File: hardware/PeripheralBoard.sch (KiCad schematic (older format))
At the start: 23 parts, among them J1 PARAM1_CV, J2 PARAM2_CV, J3 CLK/TRG, J4 DITTO, J5 OUT1, J6 OUT2, J7 B1_HDR_LEFT, J8 B1_HDR_RIGHT

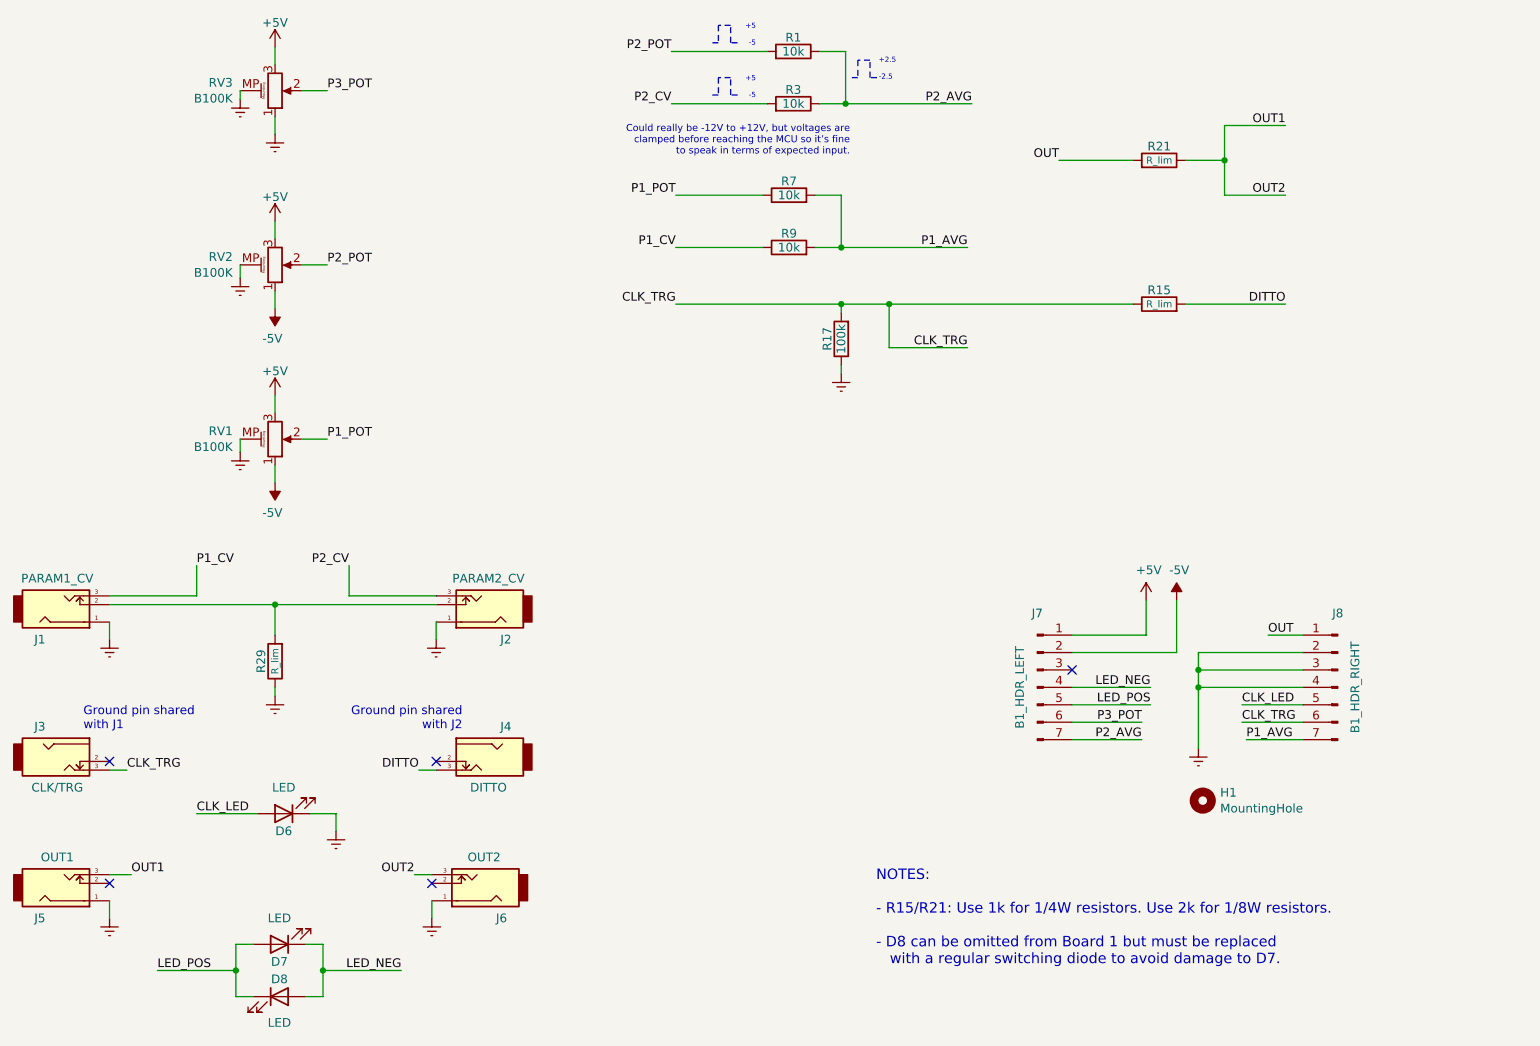
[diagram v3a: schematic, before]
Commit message: [JNTUB-HW] PCB now preparable for SMT assembly!
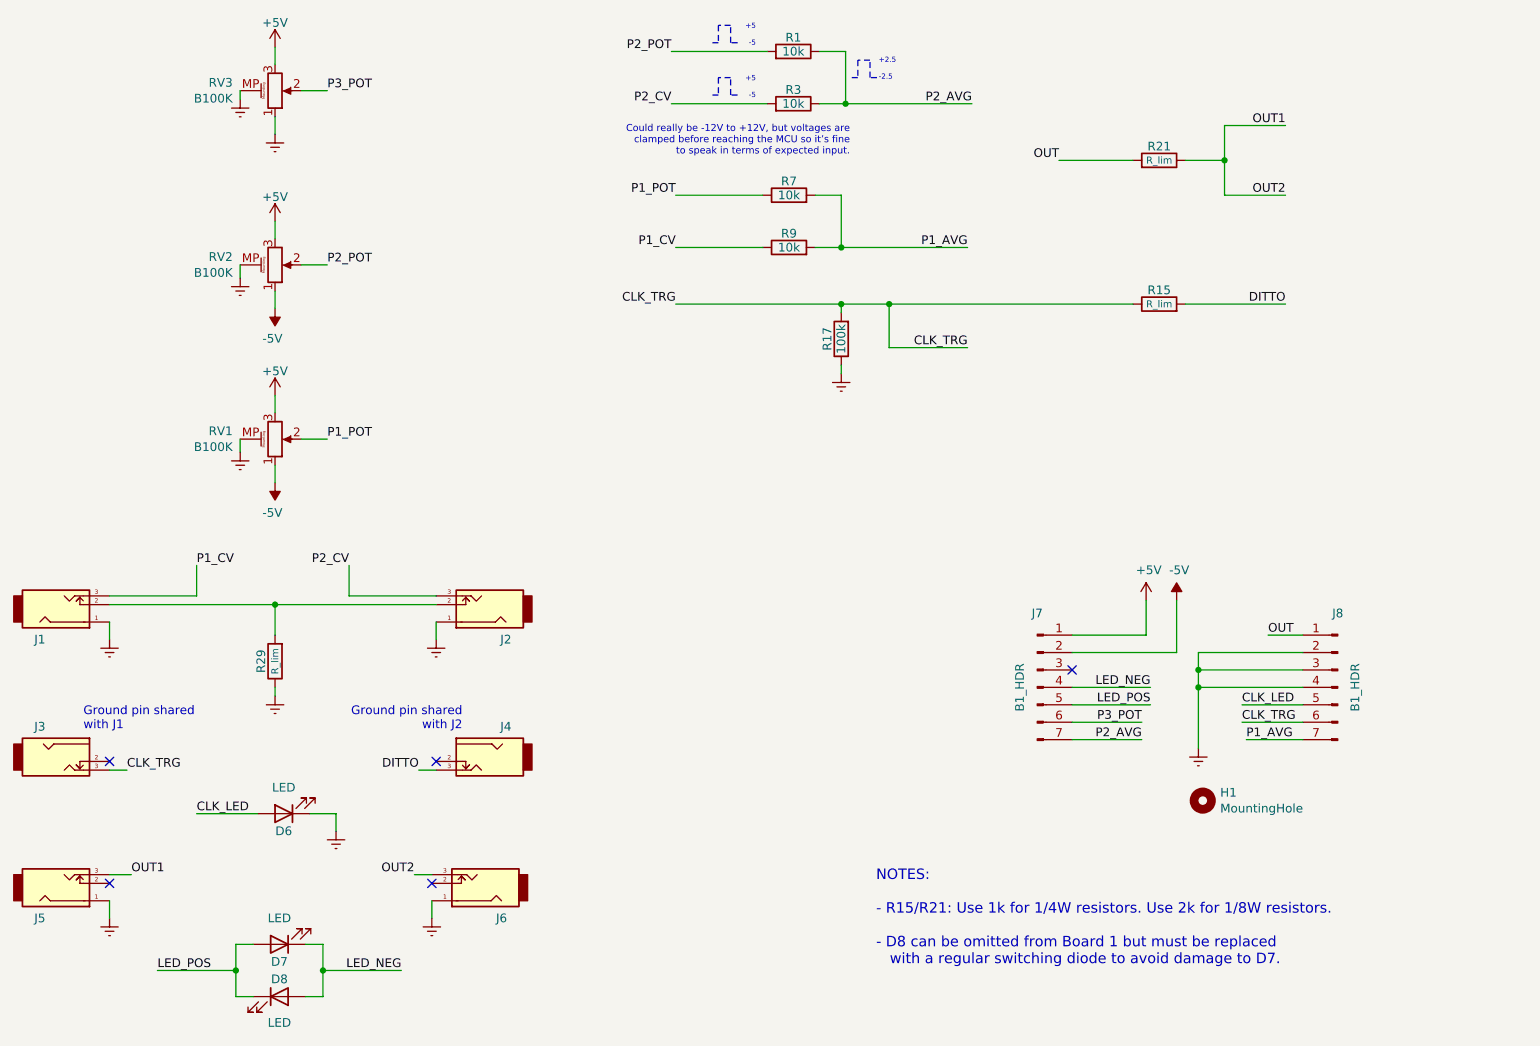
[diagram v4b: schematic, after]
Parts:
- D6, D7, D8: Config (none) -> -smtmfg; Type (none) -> 3mm LED
- H1: Config (none) -> do not fit; Exclude (none) -> Yes
- J1: value PARAM1_CV -> 3.5mm Mono Jack; Config (none) -> -smtmfg; Type (none) -> Thonkiconn Jack
- J2: value PARAM2_CV -> 3.5mm Mono Jack; Config (none) -> -smtmfg; Type (none) -> Thonkiconn Jack
- J3: value CLK/TRG -> 3.5mm Mono Jack; Config (none) -> -smtmfg; Type (none) -> Thonkiconn Jack
- J4: value DITTO -> 3.5mm Mono Jack; Config (none) -> -smtmfg; Type (none) -> Thonkiconn Jack
- J5: value OUT1 -> 3.5mm Mono Jack; Config (none) -> -smtmfg; Type (none) -> Thonkiconn Jack
- J6: value OUT2 -> 3.5mm Mono Jack; Config (none) -> -smtmfg; Type (none) -> Thonkiconn Jack
- J7: value B1_HDR_LEFT -> B1_HDR; Config (none) -> -smtmfg; Type (none) -> 1x7 Male Pin Header
- J8: value B1_HDR_RIGHT -> B1_HDR; Config (none) -> -smtmfg; Type (none) -> 1x7 Male Pin Header
- R1, R3, R7, R9: LCSC (none) -> C17414; SMT Place (none) -> Yes; SMT package (none) -> R_0805; Tolerance (none) -> 1%; Type (none) -> 1% Metal Film Resistor
- R15, R21, R29: LCSC (none) -> C4410; Note (none) -> Use 1k 1/4W or 2k 1/8W; Power Rating (none) -> 1/4W; SMT Note (none) -> 1206 1/4W; SMT Place (none) -> Yes; SMT package (none) -> R_0805 or R_1206; Type (none) -> 5% Resistor
- R17: LCSC (none) -> C17407; SMT Place (none) -> Yes; SMT package (none) -> R_0805; Type (none) -> 5% Carbon Film Resistor
- RV1, RV2, RV3: Config (none) -> -smtmfg; Type (none) -> Alpha 9mm Vertical Potentiometer
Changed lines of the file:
@@
 F 2 "SDIY:Potentiometer_Alpha_9mm_WithGround" H 3250 1450 50  0001 C CNN
 F 3 "" H 3250 1450 50  0001 C CNN
+F 4 "" H 3250 1450 50  0001 C CNN "Part"
+F 5 "-smtmfg" H 3250 1450 50  0001 C CNN "Config"
+F 6 "Alpha 9mm Vertical Potentiometer" H 3250 1450 50  0001 C CNN "Type"
 	1    3250 1450
 	1    0    0    1
@@
 F 2 "SDIY:Potentiometer_Alpha_9mm_WithGround" H 3250 2450 50  0001 C CNN
 F 3 "" H 3250 2450 50  0001 C CNN
+F 4 "" H 3250 2450 50  0001 C CNN "Part"
+F 5 "-smtmfg" H 3250 2450 50  0001 C CNN "Config"
+F 6 "Alpha 9mm Vertical Potentiometer" H 3250 2450 50  0001 C CNN "Type"
 	1    3250 2450
 	1    0    0    1
@@
 P 1850 4400
 F 0 "J1" H 1900 4200 50  0000 C CNN
-F 1 "PARAM1_CV" H 2000 4550 50  0000 C CNN
+F 1 "3.5mm Mono Jack" H 2000 4550 50  0001 C CNN
 F 2 "SDIY:PJ301M-12_Thonkiconn" H 1850 4400 50  0001 C CNN
 F 3 "" H 1850 4400 50  0001 C CNN
+F 4 "" H 1850 4400 50  0001 C CNN "Part"
+F 5 "-smtmfg" H 1850 4400 50  0001 C CNN "Config"
+F 6 "Thonkiconn Jack" H 1850 4400 50  0001 C CNN "Type"
 	1    1850 4400
 	1    0    0    -1
@@
 F 2 "SDIY:Potentiometer_Alpha_9mm_WithGround" H 3250 3450 50  0001 C CNN
 F 3 "" H 3250 3450 50  0001 C CNN
+F 4 "" H 3250 3450 50  0001 C CNN "Part"
+F 5 "-smtmfg" H 3250 3450 50  0001 C CNN "Config"
+F 6 "Alpha 9mm Vertical Potentiometer" H 3250 3450 50  0001 C CNN "Type"
 	1    3250 3450
 	1    0    0    1
@@
 P 4625 4400
 F 0 "J2" H 4675 4200 50  0000 C CNN
-F 1 "PARAM2_CV" H 4775 4550 50  0000 C CNN
+F 1 "3.5mm Mono Jack" H 4775 4550 50  0001 C CNN
 F 2 "SDIY:PJ301M-12_Thonkiconn" H 4625 4400 50  0001 C CNN
 F 3 "" H 4625 4400 50  0001 C CNN
+F 4 "" H 4625 4400 50  0001 C CNN "Part"
+F 5 "-smtmfg" H 4625 4400 50  0001 C CNN "Config"
+F 6 "Thonkiconn Jack" H 4625 4400 50  0001 C CNN "Type"
 	1    4625 4400
 	-1   0    0    -1
@@
 P 4625 5300
 F 0 "J4" H 4675 5100 50  0000 C CNN
-F 1 "DITTO" H 4775 5450 50  0000 C CNN
+F 1 "3.5mm Mono Jack" H 4775 5450 50  0001 C CNN
 F 2 "SDIY:PJ301M-12_Thonkiconn_NoGround" H 4625 5300 50  0001 C CNN
 F 3 "" H 4625 5300 50  0001 C CNN
+F 4 "" H 4625 5300 50  0001 C CNN "Part"
+F 5 "-smtmfg" H 4625 5300 50  0001 C CNN "Config"
+F 6 "Thonkiconn Jack" H 4625 5300 50  0001 C CNN "Type"
 	1    4625 5300
 	-1   0    0    1
@@
 P 1850 6000
 F 0 "J5" H 1900 5800 50  0000 C CNN
-F 1 "OUT1" H 2000 6150 50  0000 C CNN
+F 1 "3.5mm Mono Jack" H 2000 6150 50  0001 C CNN
 F 2 "SDIY:PJ301M-12_Thonkiconn" H 1850 6000 50  0001 C CNN
 F 3 "" H 1850 6000 50  0001 C CNN
+F 4 "" H 1850 6000 50  0001 C CNN "Part"
+F 5 "-smtmfg" H 1850 6000 50  0001 C CNN "Config"
+F 6 "Thonkiconn Jack" H 1850 6000 50  0001 C CNN "Type"
 	1    1850 6000
 	1    0    0    -1
@@
 P 4600 6000
 F 0 "J6" H 4650 5800 50  0000 C CNN
-F 1 "OUT2" H 4750 6150 50  0000 C CNN
+F 1 "3.5mm Mono Jack" H 4750 6150 50  0001 C CNN
 F 2 "SDIY:PJ301M-12_Thonkiconn" H 4600 6000 50  0001 C CNN
 F 3 "" H 4600 6000 50  0001 C CNN
+F 4 "" H 4600 6000 50  0001 C CNN "Part"
+F 5 "-smtmfg" H 4600 6000 50  0001 C CNN "Config"
+F 6 "Thonkiconn Jack" H 4600 6000 50  0001 C CNN "Type"
 	1    4600 6000
 	-1   0    0    -1
@@
 F 2 "LEDs:LED_D3.0mm" H 3275 6350 50  0001 C CNN
 F 3 "" H 3275 6350 50  0001 C CNN
+F 4 "" H 3275 6350 50  0001 C CNN "Part"
+F 5 "-smtmfg" H 3275 6350 50  0001 C CNN "Config"
+F 6 "3mm LED" H 3275 6350 50  0001 C CNN "Type"
 	1    3275 6350
 	-1   0    0    1
@@
 F 2 "LEDs:LED_D3.0mm" H 3275 6650 50  0001 C CNN
 F 3 "" H 3275 6650 50  0001 C CNN
+F 4 "" H 3275 6650 50  0001 C CNN "Part"
+F 5 "-smtmfg" H 3275 6650 50  0001 C CNN "Config"
+F 6 "3mm LED" H 3275 6650 50  0001 C CNN "Type"
 	1    3275 6650
 	1    0    0    -1
@@
 F 2 "LEDs:LED_D3.0mm" H 3300 5600 50  0001 C CNN
 F 3 "" H 3300 5600 50  0001 C CNN
+F 4 "" H 3300 5600 50  0001 C CNN "Part"
+F 5 "-smtmfg" H 3300 5600 50  0001 C CNN "Config"
+F 6 "3mm LED" H 3300 5600 50  0001 C CNN "Type"
 	1    3300 5600
 	-1   0    0    1
@@
 AR Path="/5FE9B0F3/61DF2F72" Ref="J7"  Part="1"
 F 0 "J7" H 7625 5300 50  0000 C CNN
-F 1 "B1_HDR_LEFT" V 7525 4875 50  0000 C CNN
+F 1 "B1_HDR" V 7525 4875 50  0000 C CNN
 F 2 "Pin_Headers:Pin_Header_Straight_1x07_Pitch2.54mm" H 7625 4875 50  0001 C CNN
 F 3 "" H 7625 4875 50  0001 C CNN
+F 4 "" H 7625 4875 50  0001 C CNN "Part"
+F 5 "-smtmfg" H 7625 4875 50  0001 C CNN "Config"
+F 6 "1x7 Male Pin Header" H 7625 4875 50  0001 C CNN "Type"
 	1    7625 4875
 	1    0    0    -1
@@
 AR Path="/5FE9B0F3/61DF2F7C" Ref="J8"  Part="1"
 F 0 "J8" H 9350 5300 50  0000 C CNN
-F 1 "B1_HDR_RIGHT" V 9250 4875 50  0000 C CNN
+F 1 "B1_HDR" V 9250 4875 50  0000 C CNN
 F 2 "Pin_Headers:Pin_Header_Straight_1x07_Pitch2.54mm" H 9350 4875 50  0001 C CNN
 F 3 "" H 9350 4875 50  0001 C CNN
+F 4 "" H 9350 4875 50  0001 C CNN "Part"
+F 5 "-smtmfg" H 9350 4875 50  0001 C CNN "Config"
+F 6 "1x7 Male Pin Header" H 9350 4875 50  0001 C CNN "Type"
 	1    9350 4875
 	-1   0    0    -1
@@
 F 2 "Mounting_Holes:MountingHole_3.2mm_M3" H 8575 5525 50  0001 C CNN
 F 3 "~" H 8575 5525 50  0001 C CNN
+F 4 "Yes" H 8575 5525 50  0001 C CNN "Exclude"
+F 5 "do not fit" H 8575 5525 50  0001 C CNN "Config"
 	1    8575 5525
 	1    0    0    -1
@@
 F 2 "SDIY:R_Axial_DIN0207_L6.3mm_D2.5mm_P2.54mm_Vertical" V 6155 1525 50  0001 C CNN
 F 3 "" H 6225 1525 50  0001 C CNN
+F 4 "" H 6225 1525 50  0001 C CNN "Part"
+F 5 "1%" H 6225 1525 50  0001 C CNN "Tolerance"
+F 6 "C17414" H 6225 1525 50  0001 C CNN "LCSC"
+F 7 "Yes" H 6225 1525 50  0001 C CNN "SMT Place"
+F 8 "R_0805" H 6225 1525 50  0001 C CNN "SMT package"
+F 9 "1% Metal Film Resistor" H 6225 1525 50  0001 C CNN "Type"
 	1    6225 1525
 	0    1    -1   0
@@
 F 2 "SDIY:R_Axial_DIN0207_L6.3mm_D2.5mm_P2.54mm_Vertical" V 6155 1225 50  0001 C CNN
 F 3 "" H 6225 1225 50  0001 C CNN
+F 4 "" H 6225 1225 50  0001 C CNN "Part"
+F 5 "1%" H 6225 1225 50  0001 C CNN "Tolerance"
+F 6 "C17414" H 6225 1225 50  0001 C CNN "LCSC"
+F 7 "Yes" H 6225 1225 50  0001 C CNN "SMT Place"
+F 8 "R_0805" H 6225 1225 50  0001 C CNN "SMT package"
+F 9 "1% Metal Film Resistor" H 6225 1225 50  0001 C CNN "Type"
 	1    6225 1225
 	0    1    -1   0
@@
 F 2 "SDIY:R_Axial_DIN0207_L6.3mm_D2.5mm_P2.54mm_Vertical" V 6130 2350 50  0001 C CNN
 F 3 "" H 6200 2350 50  0001 C CNN
+F 4 "" H 6200 2350 50  0001 C CNN "Part"
+F 5 "1%" H 6200 2350 50  0001 C CNN "Tolerance"
+F 6 "C17414" H 6200 2350 50  0001 C CNN "LCSC"
+F 7 "Yes" H 6200 2350 50  0001 C CNN "SMT Place"
+F 8 "R_0805" H 6200 2350 50  0001 C CNN "SMT package"
+F 9 "1% Metal Film Resistor" H 6200 2350 50  0001 C CNN "Type"
 	1    6200 2350
 	0    -1   -1   0
@@
 F 2 "SDIY:R_Axial_DIN0207_L6.3mm_D2.5mm_P2.54mm_Vertical" V 6130 2050 50  0001 C CNN
 F 3 "" H 6200 2050 50  0001 C CNN
+F 4 "" H 6200 2050 50  0001 C CNN "Part"
+F 5 "1%" H 6200 2050 50  0001 C CNN "Tolerance"
+F 6 "C17414" H 6200 2050 50  0001 C CNN "LCSC"
+F 7 "Yes" H 6200 2050 50  0001 C CNN "SMT Place"
+F 8 "R_0805" H 6200 2050 50  0001 C CNN "SMT package"
+F 9 "1% Metal Film Resistor" H 6200 2050 50  0001 C CNN "Type"
 	1    6200 2050
 	0    -1   -1   0
@@
 F 2 "SDIY:R_Axial_DIN0207_L6.3mm_D2.5mm_P2.54mm_Vertical" V 3180 4725 50  0001 C CNN
 F 3 "" H 3250 4725 50  0001 C CNN
+F 4 "Use 1k 1/4W or 2k 1/8W" H 3250 4725 50  0001 C CNN "Note"
+F 5 "" H 3250 4725 50  0001 C CNN "Part"
+F 6 "1/4W" H 3250 4725 50  0001 C CNN "Power Rating"
+F 7 "Yes" H 3250 4725 50  0001 C CNN "SMT Place"
+F 8 "C4410" H 3250 4725 50  0001 C CNN "LCSC"
+F 9 "1206 1/4W" H 3250 4725 50  0001 C CNN "SMT Note"
+F 10 "R_0805 or R_1206" H 3250 4725 50  0001 C CNN "SMT package"
+F 11 "5% Resistor" H 3250 4725 50  0001 C CNN "Type"
 	1    3250 4725
 	-1   0    0    1
@@
 P 1850 5300
 F 0 "J3" H 1900 5100 50  0000 C CNN
-F 1 "CLK/TRG" H 2000 5450 50  0000 C CNN
+F 1 "3.5mm Mono Jack" H 2000 5450 50  0001 C CNN
 F 2 "SDIY:PJ301M-12_Thonkiconn_NoGround" H 1850 5300 50  0001 C CNN
 F 3 "" H 1850 5300 50  0001 C CNN
+F 4 "" H 1850 5300 50  0001 C CNN "Part"
+F 5 "-smtmfg" H 1850 5300 50  0001 C CNN "Config"
+F 6 "Thonkiconn Jack" H 1850 5300 50  0001 C CNN "Type"
 	1    1850 5300
 	1    0    0    1
@@
 F 2 "SDIY:R_Axial_DIN0207_L6.3mm_D2.5mm_P2.54mm_Vertical" V 8255 2675 50  0001 C CNN
 F 3 "" H 8325 2675 50  0001 C CNN
+F 4 "Use 1k 1/4W or 2k 1/8W" H 8325 2675 50  0001 C CNN "Note"
+F 5 "" H 8325 2675 50  0001 C CNN "Part"
+F 6 "1/4W" H 8325 2675 50  0001 C CNN "Power Rating"
+F 7 "Yes" H 8325 2675 50  0001 C CNN "SMT Place"
+F 8 "C4410" H 8325 2675 50  0001 C CNN "LCSC"
+F 9 "1206 1/4W" H 8325 2675 50  0001 C CNN "SMT Note"
+F 10 "R_0805 or R_1206" H 8325 2675 50  0001 C CNN "SMT package"
+F 11 "5% Resistor" H 8325 2675 50  0001 C CNN "Type"
 	1    8325 2675
 	0    -1   -1   0
@@
 F 2 "SDIY:R_Axial_DIN0207_L6.3mm_D2.5mm_P2.54mm_Vertical" V 6430 2875 50  0001 C CNN
 F 3 "" H 6500 2875 50  0001 C CNN
+F 4 "" H 6500 2875 50  0001 C CNN "Part"
+F 5 "Yes" H 6500 2875 50  0001 C CNN "SMT Place"
+F 6 "C17407" H 6500 2875 50  0001 C CNN "LCSC"
+F 7 "R_0805" H 6500 2875 50  0001 C CNN "SMT package"
+F 8 "5% Carbon Film Resistor" H 6500 2875 50  0001 C CNN "Type"
 	1    6500 2875
 	-1   0    0    1
@@
 F 2 "SDIY:R_Axial_DIN0207_L6.3mm_D2.5mm_P2.54mm_Vertical" V 8255 1850 50  0001 C CNN
 F 3 "" H 8325 1850 50  0001 C CNN
+F 4 "Use 1k 1/4W or 2k 1/8W" H 8325 1850 50  0001 C CNN "Note"
+F 5 "" H 8325 1850 50  0001 C CNN "Part"
+F 6 "1/4W" H 8325 1850 50  0001 C CNN "Power Rating"
+F 7 "Yes" H 8325 1850 50  0001 C CNN "SMT Place"
+F 8 "C4410" H 8325 1850 50  0001 C CNN "LCSC"
+F 9 "1206 1/4W" H 8325 1850 50  0001 C CNN "SMT Note"
+F 10 "R_0805 or R_1206" H 8325 1850 50  0001 C CNN "SMT package"
+F 11 "5% Resistor" H 8325 1850 50  0001 C CNN "Type"
 	1    8325 1850
 	0    1    -1   0
